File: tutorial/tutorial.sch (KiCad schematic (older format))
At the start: 5 parts, among them J1 MYCONN3, U1 PIC12C508A-I/SN

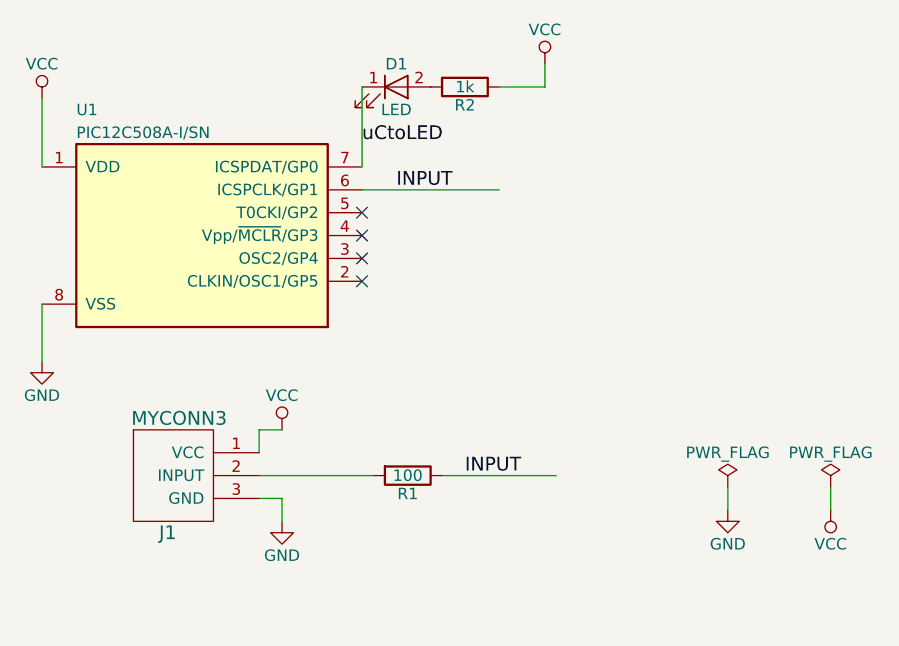
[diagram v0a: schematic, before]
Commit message: Changed to microUSB connector
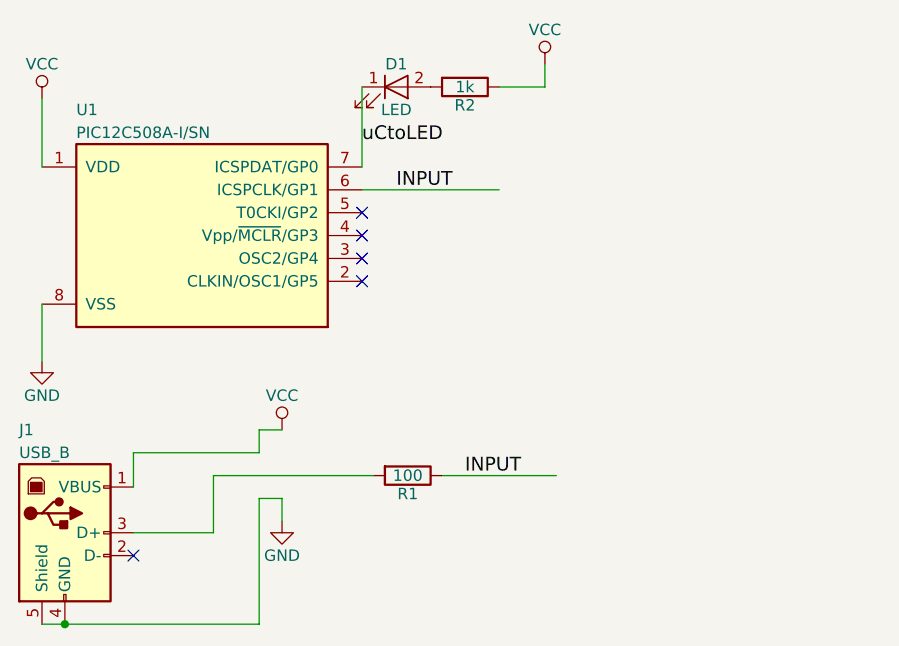
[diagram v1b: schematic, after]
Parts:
- removed J1: MYCONN3, Connectors:BARREL_JACK, symbol MYCONN3
- added J1: USB_B, Connectors:USB_Micro-B, symbol USB_B
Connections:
- wire segments 16 -> 20
- no-connect marks 4 -> 5
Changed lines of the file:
@@
-$EndComp
-$Comp
-L MYCONN3 J1
-U 1 1 59AE0ABA
-P 2150 4100
-F 0 "J1" H 2300 3550 60  0000 C CNN
-F 1 "MYCONN3" H 2350 4050 60  0000 C CNN
-F 2 "Connectors:BARREL_JACK" H 2350 3750 60  0001 C CNN
-F 3 "" H 2350 3750 60  0001 C CNN
-	1    2150 4100
-	1    0    0    -1
 $EndComp
 $Comp
@@
 	2800 4500 2800 4600
 Wire Wire Line
-	2700 4400 3200 4400
+	2500 4400 3200 4400
 Wire Wire Line
 	3950 2600 3950 2700
@@
 NoConn ~ 3150 3550
 $Comp
-L GND #PWR06
-U 1 1 59AE0EED
-P 4750 4550
-F 0 "#PWR06" H 4750 4300 50  0001 C CNN
-F 1 "GND" H 4750 4400 50  0000 C CNN
-F 2 "" H 4750 4550 50  0001 C CNN
-F 3 "" H 4750 4550 50  0001 C CNN
-	1    4750 4550
-	1    0    0    -1
-$EndComp
-$Comp
-L VCC #PWR07
-U 1 1 59AE0F07
-P 5200 4550
-F 0 "#PWR07" H 5200 4400 50  0001 C CNN
-F 1 "VCC" H 5200 4700 50  0000 C CNN
-F 2 "" H 5200 4550 50  0001 C CNN
-F 3 "" H 5200 4550 50  0001 C CNN
-	1    5200 4550
-	-1   0    0    1
-$EndComp
-$Comp
-L PWR_FLAG #FLG08
-U 1 1 59AE0F1E
-P 4750 4450
-F 0 "#FLG08" H 4750 4525 50  0001 C CNN
-F 1 "PWR_FLAG" H 4750 4600 50  0000 C CNN
-F 2 "" H 4750 4450 50  0001 C CNN
-F 3 "" H 4750 4450 50  0001 C CNN
-	1    4750 4450
-	1    0    0    -1
-$EndComp
-$Comp
-L PWR_FLAG #FLG09
-U 1 1 59AE0F3F
-P 5200 4450
-F 0 "#FLG09" H 5200 4525 50  0001 C CNN
-F 1 "PWR_FLAG" H 5200 4600 50  0000 C CNN
-F 2 "" H 5200 4450 50  0001 C CNN
-F 3 "" H 5200 4450 50  0001 C CNN
-	1    5200 4450
+L USB_B J1
+U 1 1 59AE18BE
+P 1850 4650
+F 0 "J1" H 1650 5100 50  0000 L CNN
+F 1 "USB_B" H 1650 5000 50  0000 L CNN
+F 2 "Connectors:USB_Micro-B" H 2000 4600 50  0001 C CNN
+F 3 "" H 2000 4600 50  0001 C CNN
+	1    1850 4650
 	1    0    0    -1
 $EndComp
 Wire Wire Line
-	5200 4450 5200 4550
+	2700 4300 2150 4300
 Wire Wire Line
-	4750 4450 4750 4550
+	2150 4300 2150 4450
+Wire Wire Line
+	1750 5050 2700 5050
+Wire Wire Line
+	2700 5050 2700 4500
+Connection ~ 1850 5050
+Wire Wire Line
+	2150 4650 2500 4650
+Wire Wire Line
+	2500 4650 2500 4400
+NoConn ~ 2150 4750
 $EndSCHEMATC
